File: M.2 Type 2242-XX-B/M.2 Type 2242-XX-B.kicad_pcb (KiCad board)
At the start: 2 copper layers, 22 x 42 mm, 4 parts, among them J1 Conn_Coaxial, J2 Conn_Coaxial, M1 M.2_Standoff_Card_Pad, U1 M.2_NGFF_Socket2_KeyB_SSIC_Ad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

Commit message: Add proper footprint to solder jumpers
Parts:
- J1: value Conn_Coaxial -> ANT1
- J2: value Conn_Coaxial -> ANT2
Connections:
- net Net-(J1-Pad1) renamed /Radio Tranceiver/ANT_A
- net Net-(J2-Pad1) renamed /Radio Tranceiver/ANT_B
- J1 pad 2: Net-(J1-Pad2) -> GND
- J2 pad 2: Net-(J2-Pad2) -> GND

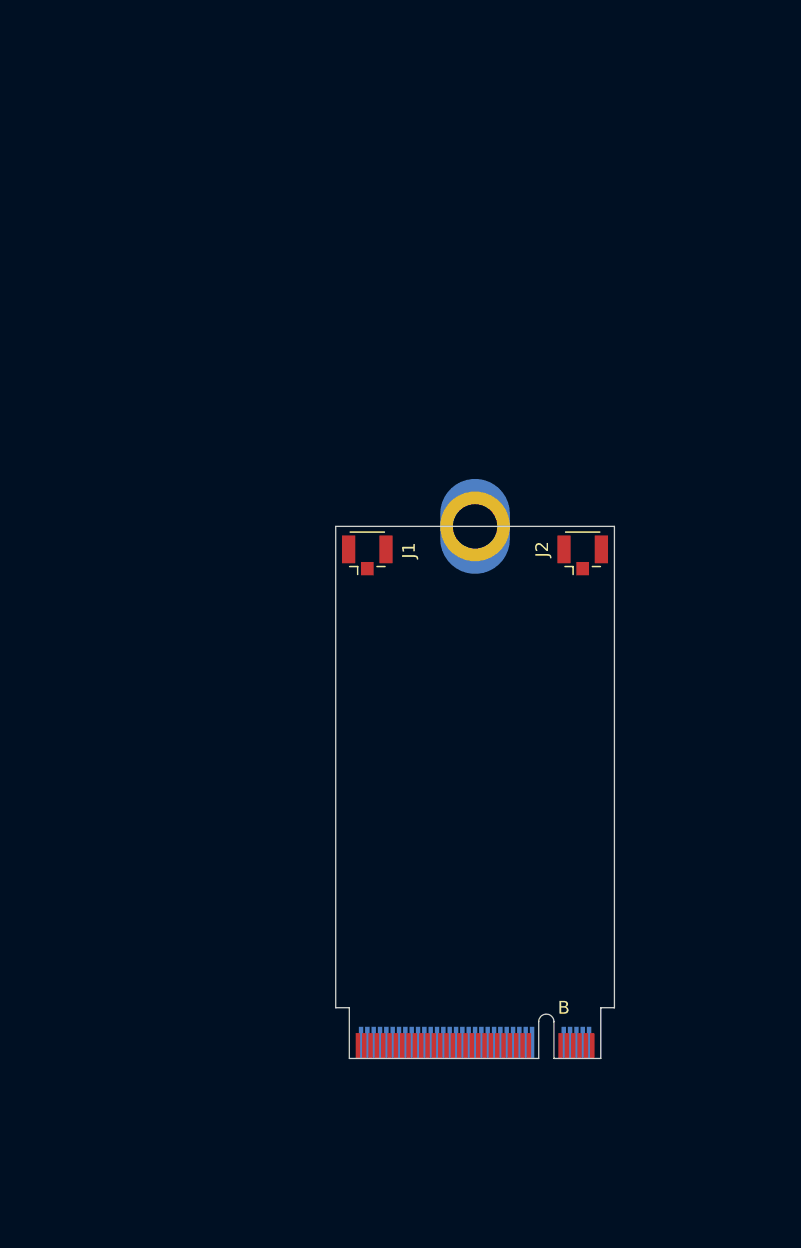
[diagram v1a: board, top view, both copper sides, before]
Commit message: Initial placement, I think we are going for the STM32F103 instead
The LQPF-100 is simply too big
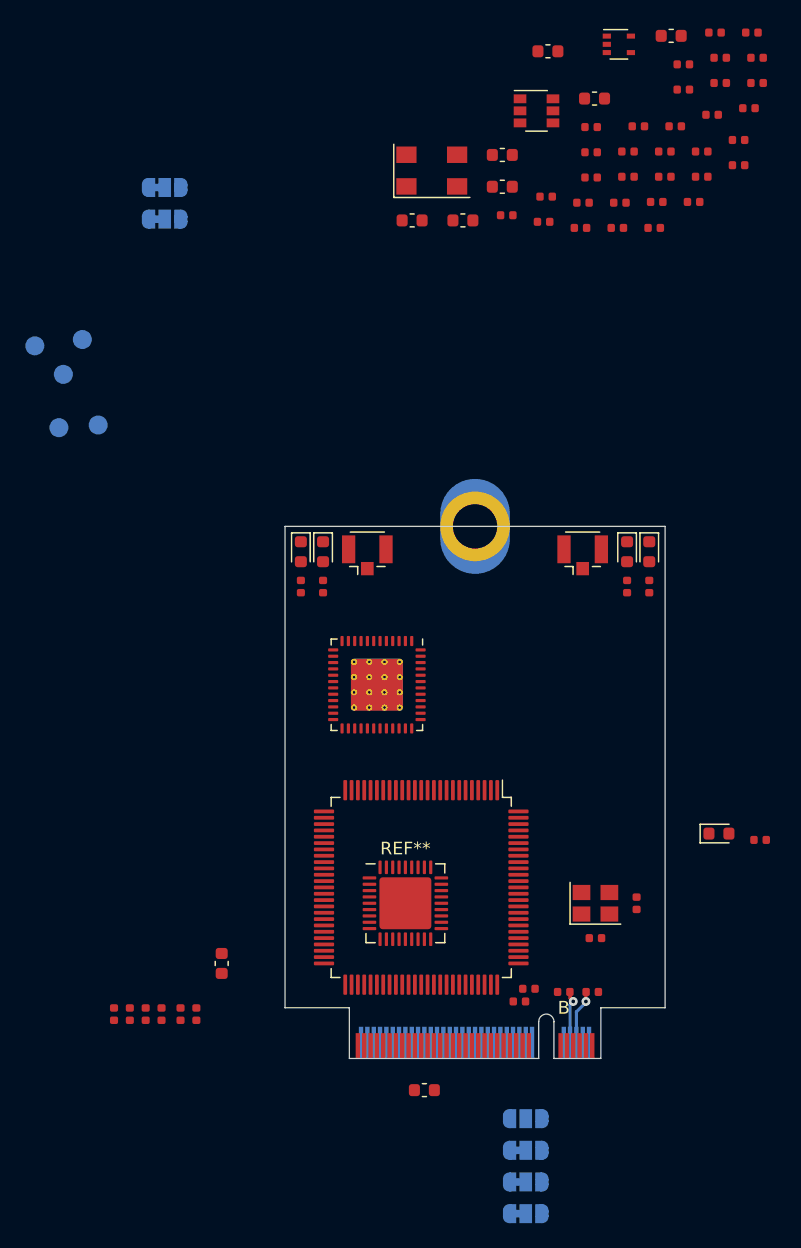
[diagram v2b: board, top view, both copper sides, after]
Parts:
- added C1: 10uF, Capacitor_SMD:C_0603_1608Metric, F.Cu at (16.8, -37.5)
- added C10: 100nF, Capacitor_SMD:C_0402_1005Metric, F.Cu at (20.2, -31.5)
- added C11: 10nF, Capacitor_SMD:C_0402_1005Metric, F.Cu at (29.9, -39.0)
- added C12: 10nF, Capacitor_SMD:C_0402_1005Metric, F.Cu at (28.9, -29.6)
- added C13: 100nF, Capacitor_SMD:C_0402_1005Metric, F.Cu at (31.8, -30.5)
- added C14: 470pF, Capacitor_SMD:C_0402_1005Metric, F.Cu at (28.2, -25.6)
- added C15: 22nF, Capacitor_SMD:C_0402_1005Metric, F.Cu at (31.8, -28.5)
- added C16: 15nF, Capacitor_SMD:C_0402_1005Metric, F.Cu at (25.1, -23.6)
- added C17: 1nF, Capacitor_SMD:C_0402_1005Metric, F.Cu at (16.4, -24.0)
- added C18: 22pF, Capacitor_SMD:C_0402_1005Metric, F.Cu at (20.2, -27.5)
- added C19: 10nF, Capacitor_SMD:C_0402_1005Metric, F.Cu at (13.5, -24.6)
- added C2: 100pF, Capacitor_SMD:C_0402_1005Metric, F.Cu at (22.4, -25.6)
- added C20: 100nF, Capacitor_SMD:C_0402_1005Metric, F.Cu at (32.9, -39.0)
- added C21: 100nF, Capacitor_SMD:C_0402_1005Metric, F.Cu at (23.1, -27.6)
- added C22: 10nF, Capacitor_SMD:C_0402_1005Metric, F.Cu at (26.8, -31.6)
- added C23: 10nF, Capacitor_SMD:C_0402_1005Metric, F.Cu at (30.4, -37.0)
- added C24: 27pF, Capacitor_SMD:C_0402_1005Metric, F.Cu at (20.5, 32.5)
- added C25: 27pF, Capacitor_SMD:C_0402_1005Metric, F.Cu at (23.8, 29.8)
- added C26: 2.2µF, Capacitor_SMD:C_0603_1608Metric, F.Cu at (-9.00, 34.5)
- added C27: 2.2µF, Capacitor_SMD:C_0603_1608Metric, F.Cu at (7.00, 44.5)
- added C28: 100n, Capacitor_SMD:C_0402_1005Metric, F.Cu at (-16.2, 38.5)
- added C29: 100n, Capacitor_SMD:C_0402_1005Metric, F.Cu at (-13.8, 38.5)
- added C3: 100pF, Capacitor_SMD:C_0402_1005Metric, F.Cu at (19.5, -25.6)
- added C30: 100n, Capacitor_SMD:C_0402_1005Metric, F.Cu at (-17.5, 38.5)
- added C31: 100n, Capacitor_SMD:C_0402_1005Metric, F.Cu at (-15.0, 38.5)
- added C32: 100n, Capacitor_SMD:C_0402_1005Metric, F.Cu at (-11.0, 38.5)
- added C33: 100n, Capacitor_SMD:C_0402_1005Metric, F.Cu at (-12.2, 38.5)
- added C34: 6.8pF, Capacitor_SMD:C_0402_1005Metric, F.Cu at (19.3, -23.6)
- added C35: C, Capacitor_SMD:C_0402_1005Metric, F.Cu at (33.3, -37.0)
- added C36: 11pF, Capacitor_SMD:C_0402_1005Metric, F.Cu at (26.0, -29.6)
- added C4: C, Capacitor_SMD:C_0402_1005Metric, F.Cu at (23.1, -29.6)
- added C5: 100pF, Capacitor_SMD:C_0402_1005Metric, F.Cu at (27.4, -34.5)
- added C6: 10nF, Capacitor_SMD:C_0402_1005Metric, F.Cu at (27.4, -36.5)
- added C7: 11pF, Capacitor_SMD:C_0402_1005Metric, F.Cu at (23.9, -31.6)
- added C8: 220pF, Capacitor_SMD:C_0402_1005Metric, F.Cu at (16.6, -26.0)
- added C9: 11pF, Capacitor_SMD:C_0402_1005Metric, F.Cu at (20.2, -29.5)
- added D1: LED_A_TX, LED_SMD:LED_0603_1608Metric, F.Cu at (-2.75, 2.00)
- added D2: LED0, LED_SMD:LED_0603_1608Metric, F.Cu at (30.2, 24.2)
- added D3: LED_A_RX, LED_SMD:LED_0603_1608Metric, F.Cu at (-1.00, 2.00)
- added D4: LED_B_TX, LED_SMD:LED_0603_1608Metric, F.Cu at (24.8, 2.00)
- added D5: LED_B_RX, LED_SMD:LED_0603_1608Metric, F.Cu at (23.0, 2.00)
- added JP1: CONFIG_0, Jumper:SolderJumper-3_P1.3mm_Bridged12_RoundedPad1.0x1.5mm, B.Cu at (15.0, 51.8)
- added JP2: CONFIG_1, Jumper:SolderJumper-3_P1.3mm_Bridged12_RoundedPad1.0x1.5mm, B.Cu at (15.0, 49.2)
- added JP3: CONFIG_2, Jumper:SolderJumper-3_P1.3mm_Bridged12_RoundedPad1.0x1.5mm, B.Cu at (15.0, 54.2)
- added JP4: CONFIG_3, Jumper:SolderJumper-3_P1.3mm_Open_RoundedPad1.0x1.5mm, B.Cu at (15.0, 46.8)
- added L1: 180nH, Inductor_SMD:L_0603_1608Metric, F.Cu at (13.2, -26.8)
- added L2: 68nH, Inductor_SMD:L_0603_1608Metric, F.Cu at (20.4, -33.8)
- added L3: 17nH, Inductor_SMD:L_0603_1608Metric, F.Cu at (26.5, -38.7)
- added L4: 0R, Inductor_SMD:L_0603_1608Metric, F.Cu at (10.0, -24.1)
- added L5: 22nH, Inductor_SMD:L_0603_1608Metric, F.Cu at (6.03, -24.1)
- added L6: 20nH, Inductor_SMD:L_0603_1608Metric, F.Cu at (13.2, -29.3)
- added R1: 1K1, Resistor_SMD:R_0402_1005Metric, F.Cu at (29.7, -32.5)
- added R15: 20R, Resistor_SMD:R_0402_1005Metric, F.Cu at (15.2, 36.5)
- added R16: 20R, Resistor_SMD:R_0402_1005Metric, F.Cu at (14.5, 37.5)
- added R17: 10K, Resistor_SMD:R_0402_1005Metric, F.Cu at (-2.75, 4.75)
- added R18: 10K, Resistor_SMD:R_0402_1005Metric, F.Cu at (33.5, 24.8)
- added R19: 10K, Resistor_SMD:R_0402_1005Metric, F.Cu at (-1.00, 4.75)
- added R2: 3R9, Resistor_SMD:R_0402_1005Metric, F.Cu at (26.0, -27.6)
- added R20: 10K, Resistor_SMD:R_0402_1005Metric, F.Cu at (24.8, 4.75)
- added R21: 10K, Resistor_SMD:R_0402_1005Metric, F.Cu at (23.0, 4.75)
- added R22: 200K, Resistor_SMD:R_0402_1005Metric, F.Cu at (18.0, 36.8)
- added R23: 200K, Resistor_SMD:R_0402_1005Metric, F.Cu at (20.2, 36.8)
- added R3: 3K6, Resistor_SMD:R_0402_1005Metric, F.Cu at (33.3, -35.0)
- added R4: 560R, Resistor_SMD:R_0402_1005Metric, F.Cu at (22.2, -23.6)
- added R5: 270R, Resistor_SMD:R_0402_1005Metric, F.Cu at (30.4, -35.0)
- added R6: 1K, Resistor_SMD:R_0402_1005Metric, F.Cu at (25.3, -25.6)
- added R7: 1K, Resistor_SMD:R_0402_1005Metric, F.Cu at (32.6, -33.0)
- added R8: 1K, Resistor_SMD:R_0402_1005Metric, F.Cu at (28.9, -27.6)
- added REF**: QFN-36-1EP_6x6mm_P0.5mm_EP4.1x4.1mm, Package_DFN_QFN:QFN-36-1EP_6x6mm_P0.5mm_EP4.1x4.1mm, F.Cu at (5.50, 29.8)
- added SJ1: BOOT0, Jumper:SolderJumper-3_P1.3mm_Bridged12_RoundedPad1.0x1.5mm, B.Cu at (-13.5, -24.2)
- added SJ2: BOOT1, Jumper:SolderJumper-3_P1.3mm_Bridged12_RoundedPad1.0x1.5mm, B.Cu at (-13.5, -26.8)
- added TP1: FILT_I, TestPoint:TestPoint_Pad_D1.5mm, B.Cu at (-21.9, -7.79)
- added TP2: ~FILT_I, TestPoint:TestPoint_Pad_D1.5mm, B.Cu at (-18.8, -8.00)
- added TP3: TX, TestPoint:TestPoint_Pad_D1.5mm, B.Cu at (-20.0, -14.8)
- added TP4: RX, TestPoint:TestPoint_Pad_D1.5mm, B.Cu at (-23.8, -14.2)
- added TP5: GND, TestPoint:TestPoint_Pad_D1.5mm, B.Cu at (-21.5, -12.0)
- added U2: AS193-73, Package_TO_SOT_SMD:SuperSOT-6, F.Cu at (15.8, -32.8)
- added U3: M74VHC1GT04DFT1G, Package_TO_SOT_SMD:SOT-353_SC-70-5, F.Cu at (22.4, -38.0)
- added U4: ADF7021BCPZ, Package_CSP:LFCSP-48-1EP_7x7mm_P0.5mm_EP4.1x4.1mm_ThermalVias, F.Cu at (3.25, 12.5)
- added U5: STM32F407VGTx, Package_QFP:LQFP-100_14x14mm_P0.5mm, F.Cu at (6.75, 28.5)
- added X1: FT5HNBPK19.44-T1, aausat:FOX924, F.Cu at (7.58, -28.1)
- added Y1: 12MHz, Crystal:Crystal_SMD_3225-4Pin_3.2x2.5mm, F.Cu at (20.5, 29.8)
- M1: value M.2_Standoff_Card_Pad -> MountingHole_Pad
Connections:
- M1 pad 1: (no net) -> GND
- U1 pad 1: Net-(U1-Pad1) -> /M.2 NGFF Fingers/CONFIG_3
- U1 pad 10: Net-(U1-Pad10) -> /Microcontroller/LED1
- U1 pad 11: Net-(U1-Pad11) -> GND
- U1 pad 21: Net-(U1-Pad21) -> /M.2 NGFF Fingers/CONFIG_0
- U1 pad 27: Net-(U1-Pad27) -> GND
- U1 pad 30: Net-(U1-Pad30) -> /Microcontroller/STM_RESET
- U1 pad 32: Net-(U1-Pad32) -> /Microcontroller/SWCLK
- U1 pad 34: Net-(U1-Pad34) -> /Microcontroller/SWDIO
- U1 pad 36: Net-(U1-Pad36) -> /Microcontroller/UART4_TX
- U1 pad 67: Net-(U1-Pad67) -> /M.2 NGFF Fingers/RESET#
- U1 pad 69: Net-(U1-Pad69) -> /M.2 NGFF Fingers/CONFIG_1
- U1 pad 7: Net-(U1-Pad7) -> /M.2 NGFF Fingers/USB_D+
- U1 pad 75: Net-(U1-Pad75) -> /M.2 NGFF Fingers/CONFIG_2
- U1 pad 9: Net-(U1-Pad9) -> /M.2 NGFF Fingers/USB_D-
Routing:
- net Net-(R23-Pad1): track 0.00 -> 4.32 mm, vias 0 -> 1
- net Net-(R22-Pad2): track 0.00 -> 4.21 mm, vias 0 -> 1
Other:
- board size 22 x 42 mm -> 30 x 42 mm
- net class Default: via_dia 0.8 -> 0.7; via_drill 0.4 -> 0.3
- board text added: "Board thickness should be 0.8 mm! If this was not selected when ordering, STOP, and turn back to customer."

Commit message: Schematic updated to STM32F103
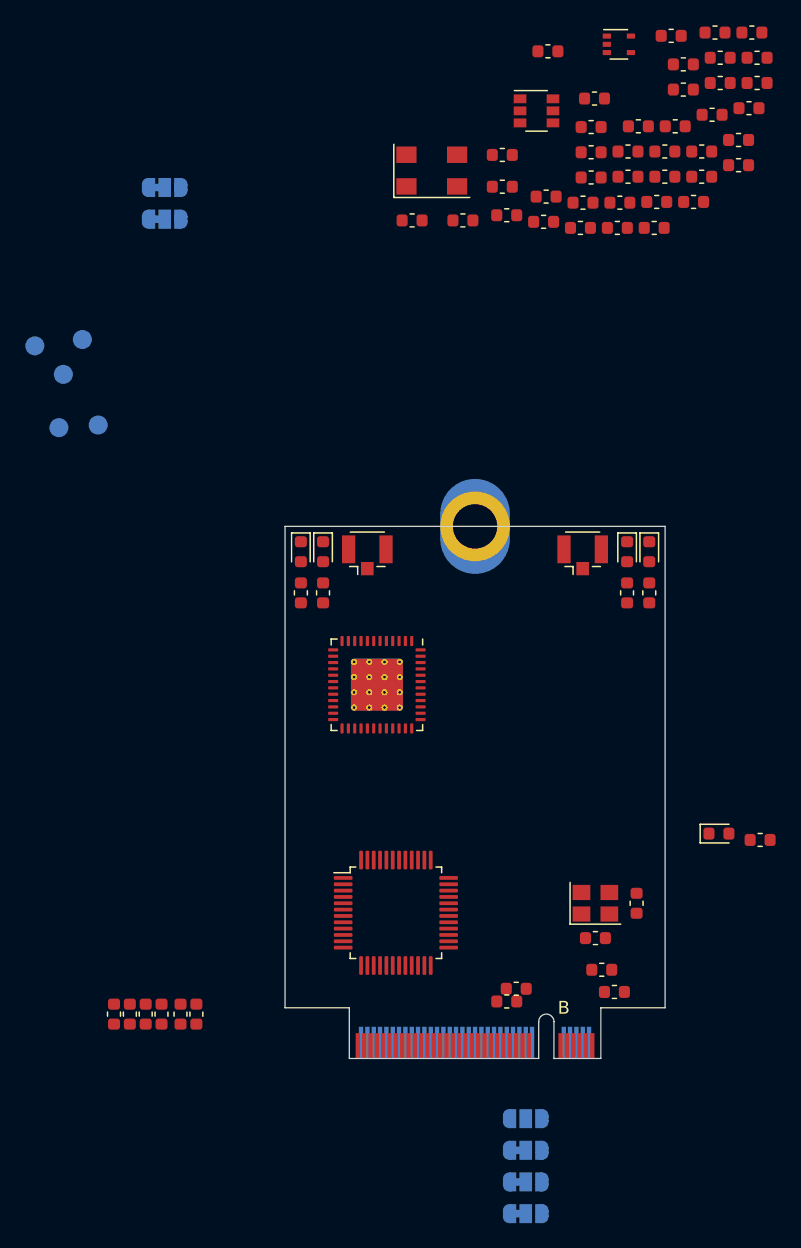
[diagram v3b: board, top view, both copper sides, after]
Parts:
- removed C26, C27: 2.2µF, Capacitor_SMD:C_0603_1608Metric
- removed REF**: QFN-36-1EP_6x6mm_P0.5mm_EP4.1x4.1mm, Package_DFN_QFN:QFN-36-1EP_6x6mm_P0.5mm_EP4.1x4.1mm
- C10, C11, C12, C13, C14, C15, C16, C17, C18, C19, C2, C20, C21, C22, C23, C24, C25, C28, C29, C3, C30, C31, C32, C33, C34, C35, C36, C4, C5, C6, C7, C8, C9: footprint Capacitor_SMD:C_0402_1005Metric -> Capacitor_SMD:C_0603_1608Metric
- R1, R15, R16, R17, R18, R19, R2, R20, R21, R22, R23, R3, R4, R5, R6, R7, R8: footprint Resistor_SMD:R_0402_1005Metric -> Resistor_SMD:R_0603_1608Metric
- U5: value STM32F407VGTx -> STM32F103C8Tx; footprint Package_QFP:LQFP-100_14x14mm_P0.5mm -> Package_QFP:LQFP-48_7x7mm_P0.5mm
- moved R22 3.47 mm to (21.0, 35.0), turned to 180 degrees
- moved U5 2.83 mm to (4.75, 30.5), turned to 0 degrees
- moved R23 1.75 mm to (22.0, 36.8)
- moved R15 1.00 mm to (14.2, 36.5)
- moved R16 1.00 mm to (13.5, 37.5)
- moved R17 0.50 mm to (-2.75, 5.25)
- moved R19 0.50 mm to (-1.00, 5.25)
- moved R20 0.50 mm to (24.8, 5.25)
- moved R21 0.50 mm to (23.0, 5.25)
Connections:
- SJ1 pad 2: Net-(SJ1-Pad2) -> /Microcontroller/BOOT0
- TP3 pad 1: /Microcontroller/UART4_TX -> /Microcontroller/UART_TX
- TP4 pad 1: /Microcontroller/UART4_RX -> /Microcontroller/UART1_RX
- U1 pad 36: /Microcontroller/UART4_TX -> /Microcontroller/UART_TX
- U5 pad 1: Net-(U5-Pad1) -> +3V3
- U5 pad 10: GND -> Net-(U5-Pad10)
- U5 pad 11: +3V3 -> /Microcontroller/ADF1_CE
- U5 pad 12: Net-(C24-Pad1) -> /Microcontroller/ADF1_SREAD
- U5 pad 13: Net-(C25-Pad1) -> /Microcontroller/ADF1_SLE
- U5 pad 14: /Microcontroller/STM_RESET -> /Microcontroller/ADF1_SDATA
- U5 pad 15: Net-(U5-Pad15) -> /Microcontroller/ADF1_SCLK
- U5 pad 16: Net-(U5-Pad16) -> /Microcontroller/ADF1_ANT_SELECT
- U5 pad 17: /Microcontroller/ADF1_TEST_A -> /Microcontroller/ADF1_SWD
- U5 pad 19: +3V3 -> /Microcontroller/LED1
- U5 pad 2: Net-(U5-Pad2) -> /Microcontroller/LED0
- U5 pad 20: GND -> /Microcontroller/BOOT1
- U5 pad 22: +3V3 -> /Microcontroller/LED_A_TX
- U5 pad 23: Net-(U5-Pad23) -> GND
- U5 pad 24: /Microcontroller/ADF1_CE -> +3V3
- U5 pad 25: /Microcontroller/ADF1_SREAD -> /Microcontroller/LED_A_RX
- U5 pad 26: /Microcontroller/ADF1_SLE -> /Microcontroller/LED_B_TX
- U5 pad 27: GND -> /Microcontroller/LED_B_RX
- U5 pad 28: +3V3 -> /M.2 NGFF Fingers/RESET#
- U5 pad 29: /Microcontroller/ADF1_SDATA -> /Microcontroller/ADF1_TEST_A
- U5 pad 30: /Microcontroller/ADF1_SCLK -> /Microcontroller/UART_TX
- U5 pad 31: Net-(U5-Pad31) -> /Microcontroller/UART1_RX
- U5 pad 32: /Radio Tranceiver/ADF_DATA_IO -> /Microcontroller/USB_OTG_FS_D-
- U5 pad 33: /Microcontroller/ADF1_MUXOUT -> /Microcontroller/USB_OTG_FS_D+
- U5 pad 34: Net-(U5-Pad34) -> /Microcontroller/SWDIO
- U5 pad 35: Net-(U5-Pad35) -> GND
- U5 pad 36: Net-(U5-Pad36) -> +3V3
- U5 pad 37: /Microcontroller/BOOT1 -> /Microcontroller/SWCLK
- U5 pad 38: /Microcontroller/LED_B_RX -> /Microcontroller/ADF1_MUXOUT
- U5 pad 39: Net-(U5-Pad39) -> /Radio Tranceiver/ADF_CLKOUT
- U5 pad 40: /Microcontroller/LED_A_TX -> /Radio Tranceiver/ADF_DATA_CLK
- U5 pad 41: /Microcontroller/LED_A_RX -> /Radio Tranceiver/ADF_DATA_IO
- U5 pad 44: Net-(U5-Pad44) -> /Microcontroller/BOOT0
- U5 pad 47: Net-(U5-Pad47) -> GND
- U5 pad 48: Net-(U5-Pad48) -> +3V3
- U5 pad 5: /Microcontroller/LED_B_TX -> Net-(C24-Pad1)
- U5 pad 6: +3V3 -> Net-(C25-Pad1)
- U5 pad 7: Net-(U5-Pad7) -> /Microcontroller/STM_RESET
- U5 pad 8: Net-(U5-Pad8) -> GND
- U5 pad 9: Net-(U5-Pad9) -> +3V3
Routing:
- net Net-(R23-Pad1): track 4.32 -> 0.00 mm, vias 1 -> 0
- net Net-(R22-Pad2): track 4.21 -> 0.00 mm, vias 1 -> 0
